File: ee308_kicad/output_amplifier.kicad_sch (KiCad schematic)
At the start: 39 parts, among them J1 Conn_Coaxial, Q1 2N3904, Q2 2N3904, Q3 2N3904, Q4 2N3906, Q5 2N3904, Q6 2N3904, Q7 2N3906

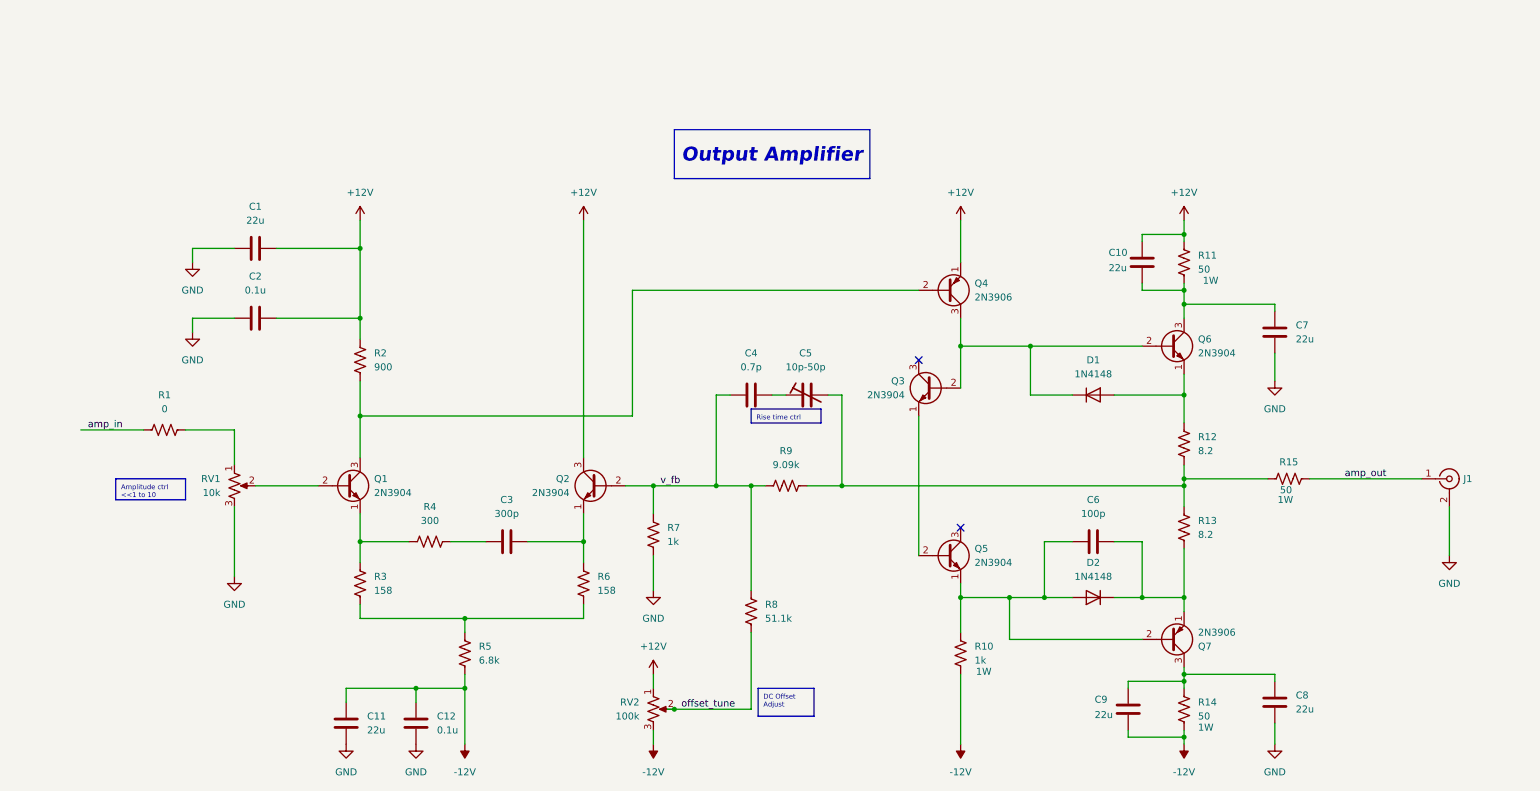
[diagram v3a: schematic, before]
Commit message: Update with current switch/integrator.
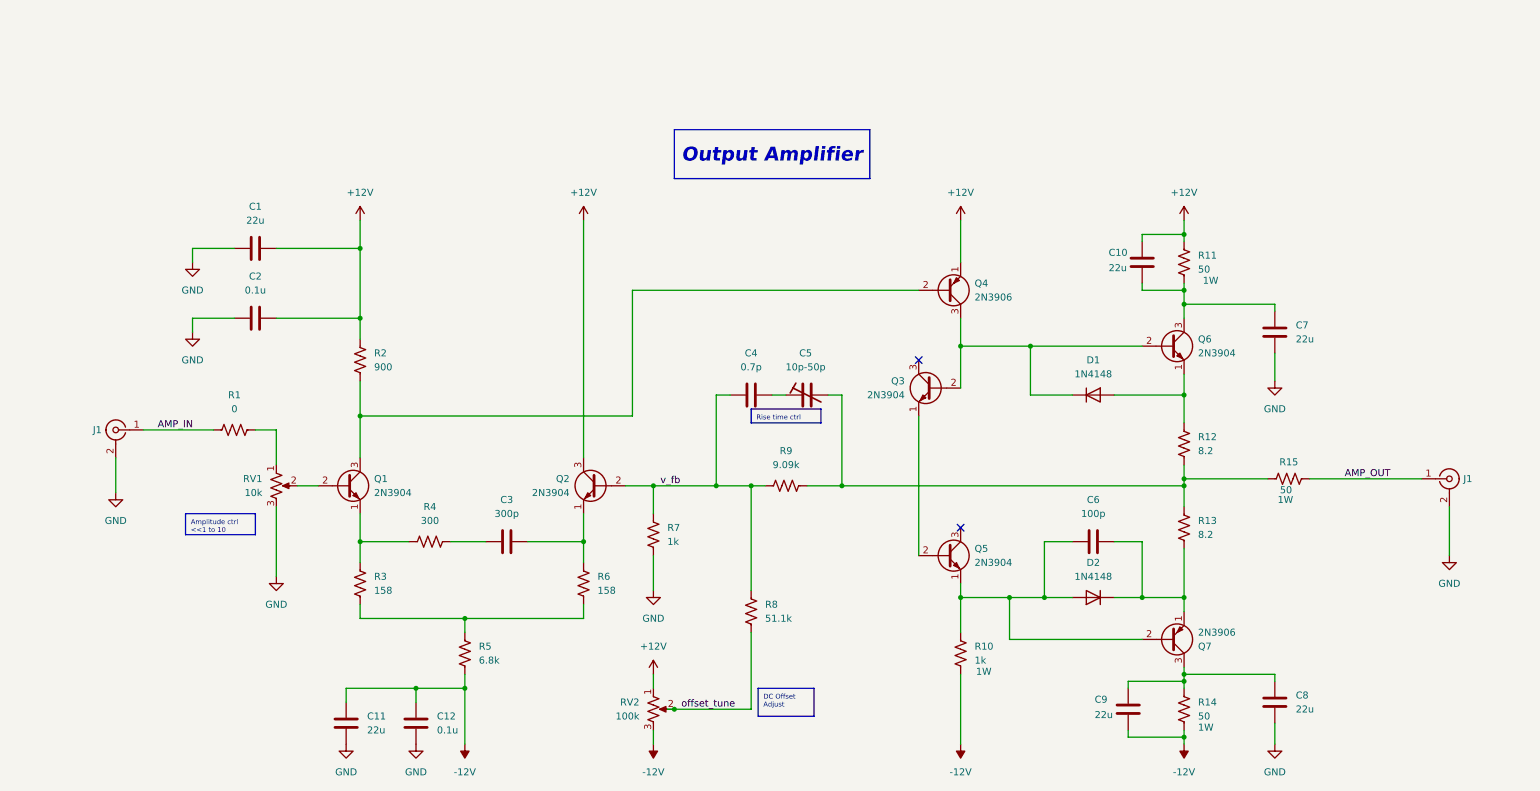
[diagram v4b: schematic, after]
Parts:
- added J1: Conn_Coaxial, Connector_Coaxial:SMA_Amphenol_901-143_Horizontal, symbol Connector:Conn_Coaxial
- J1: footprint Connector_Coaxial:BNC_TEConnectivity_1478035_Horizontal -> Connector_Coaxial:SMA_Amphenol_901-143_Horizontal
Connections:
- net GND: now also J1.2 (Ext)
- net amp_in renamed AMP_IN
- net AMP_IN: now also J1.1 (In)
- net amp_out renamed AMP_OUT
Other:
- moved on the sheet: R1, RV1
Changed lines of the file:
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@@
 	(text_box "Amplitude ctrl\n<<1 to 10"
 		(exclude_from_sim no)
-		(at 29.21 99.06 0)
+		(at 41.91 105.41 0)
 		(size 12.7 3.81)
 		(margins 0.9525 0.9525 0.9525 0.9525)
@@
 	(wire
 		(pts
-			(xy 50.8 90.17) (xy 50.8 96.52)
+			(xy 58.42 90.17) (xy 58.42 96.52)
 		)
 		(stroke
@@
 	(wire
 		(pts
-			(xy 22.86 90.17) (xy 34.29 90.17)
-		)
-		(stroke
-			(width 0)
-			(type default)
-		)
-	)
-	(wire
-		(pts
 			(xy 223.52 146.05) (xy 223.52 147.32)
 		)
@@
 	(wire
 		(pts
-			(xy 54.61 100.33) (xy 66.04 100.33)
+			(xy 62.23 100.33) (xy 66.04 100.33)
 		)
 		(stroke
@@
 	(wire
 		(pts
-			(xy 41.91 90.17) (xy 50.8 90.17)
+			(xy 34.29 90.17) (xy 46.99 90.17)
 		)
 		(stroke
@@
 	(wire
 		(pts
+			(xy 54.61 90.17) (xy 58.42 90.17)
+		)
+		(stroke
+			(width 0)
+			(type default)
+		)
+	)
+	(wire
+		(pts
 			(xy 114.3 105.41) (xy 114.3 110.49)
 		)
@@
 	(wire
 		(pts
-			(xy 50.8 104.14) (xy 50.8 116.84)
+			(xy 58.42 104.14) (xy 58.42 116.84)
 		)
 		(stroke
@@
 	(wire
 		(pts
+			(xy 29.21 95.25) (xy 29.21 101.6)
+		)
+		(stroke
+			(width 0)
+			(type default)
+		)
+	)
+	(wire
+		(pts
 			(xy 92.71 137.16) (xy 92.71 147.32)
 		)
@@
 		)
 	)
-	(label "amp_in"
-		(at 24.13 90.17 0)
+	(label "AMP_IN"
+		(at 36.83 90.17 0)
 		(effects
 			(font
@@
 		)
 	)
-	(label "amp_out"
+	(label "AMP_OUT"
 		(at 252.73 99.06 0)
 		(effects
@@
 	)
 	(symbol
+		(lib_id "Connector:Conn_Coaxial")
+		(at 29.21 90.17 0)
+		(mirror y)
+		(unit 1)
+		(exclude_from_sim no)
+		(in_bom yes)
+		(on_board yes)
+		(dnp no)
+		(property "Reference" "J1"
+			(at 26.67 90.17 0)
+			(effects
+				(font
+					(size 1.27 1.27)
+				)
+				(justify left)
+			)
+		)
+		(property "Value" "Conn_Coaxial"
+			(at 25.4 91.7331 0)
+			(effects
+				(font
+					(size 1.27 1.27)
+				)
+				(justify left)
+				(hide yes)
+			)
+		)
+		(property "Footprint" "Connector_Coaxial:SMA_Amphenol_901-143_Horizontal"
+			(at 29.21 90.17 0)
+			(effects
+				(font
+					(size 1.27 1.27)
+				)
+				(hide yes)
+			)
+		)
+		(property "Datasheet" "~"
+			(at 29.21 90.17 0)
+			(effects
+				(font
+					(size 1.27 1.27)
+				)
+				(hide yes)
+			)
+		)
+		(property "Description" "coaxial connector (BNC, SMA, SMB, SMC, Cinch/RCA, LEMO, ...)"
+			(at 29.21 90.17 0)
+			(effects
+				(font
+					(size 1.27 1.27)
+				)
+				(hide yes)
+			)
+		)
+		(pin "1"
+		)
+		(pin "2"
+		)
+		(instances
+			(project "ee308_kicad"
+				(path "/a3231158-6fd4-4190-9d01-56c0026ed088/88a04215-6888-4715-acfc-eedd1a2f0861"
+					(reference "J1")
+					(unit 1)
+				)
+			)
+		)
+	)
+	(symbol
 		(lib_id "power:GND")
 		(at 271.78 113.03 0)
@@
 	(symbol
 		(lib_id "power:GND")
-		(at 50.8 116.84 0)
+		(at 58.42 116.84 0)
 		(unit 1)
 		(exclude_from_sim no)
@@
 		(fields_autoplaced yes)
 		(property "Reference" "#PWR03"
-			(at 50.8 123.19 0)
+			(at 58.42 123.19 0)
 			(effects
 				(font
@@
 		)
 		(property "Value" "GND"
-			(at 50.8 121.92 0)
+			(at 58.42 121.92 0)
 			(effects
 				(font
@@
 		)
 		(property "Footprint" ""
-			(at 50.8 116.84 0)
+			(at 58.42 116.84 0)
 			(effects
 				(font
@@
 		)
 		(property "Datasheet" ""
-			(at 50.8 116.84 0)
+			(at 58.42 116.84 0)
 			(effects
 				(font
@@
 		)
 		(property "Description" "Power symbol creates a global label with name \"GND\" , ground"
-			(at 50.8 116.84 0)
+			(at 58.42 116.84 0)
 			(effects
 				(font
@@
 	(symbol
 		(lib_id "Device:R_Potentiometer_US")
-		(at 50.8 100.33 0)
+		(at 58.42 100.33 0)
 		(unit 1)
 		(exclude_from_sim no)
@@
 		(fields_autoplaced yes)
 		(property "Reference" "RV1"
-			(at 48.26 99.0599 0)
+			(at 55.88 99.0599 0)
 			(effects
 				(font
@@
 		)
 		(property "Value" "10k"
-			(at 48.26 101.5999 0)
+			(at 55.88 101.5999 0)
 			(effects
 				(font
@@
 		)
 		(property "Footprint" "Potentiometer_SMD:Potentiometer_ACP_CA6-VSMD_Vertical"
-			(at 50.8 100.33 0)
+			(at 58.42 100.33 0)
 			(effects
 				(font
@@
 		)
 		(property "Datasheet" "~"
-			(at 50.8 100.33 0)
+			(at 58.42 100.33 0)
 			(effects
 				(font
@@
 		)
 		(property "Description" "Potentiometer, US symbol"
-			(at 50.8 100.33 0)
+			(at 58.42 100.33 0)
 			(effects
 				(font
@@
 			)
 		)
-		(property "Footprint" "Connector_Coaxial:BNC_TEConnectivity_1478035_Horizontal"
+		(property "Footprint" "Connector_Coaxial:SMA_Amphenol_901-143_Horizontal"
 			(at 271.78 99.06 0)
 			(effects
@@
 	)
 	(symbol
+		(lib_id "power:GND")
+		(at 29.21 101.6 0)
+		(unit 1)
+		(exclude_from_sim no)
+		(in_bom yes)
+		(on_board yes)
+		(dnp no)
+		(fields_autoplaced yes)
+		(property "Reference" "#PWR035"
+			(at 29.21 107.95 0)
+			(effects
+				(font
+					(size 1.27 1.27)
+				)
+				(hide yes)
+			)
+		)
+		(property "Value" "GND"
+			(at 29.21 106.68 0)
+			(effects
+				(font
+					(size 1.27 1.27)
+				)
+			)
+		)
+		(property "Footprint" ""
+			(at 29.21 101.6 0)
+			(effects
+				(font
+					(size 1.27 1.27)
+				)
+				(hide yes)
+			)
+		)
+		(property "Datasheet" ""
+			(at 29.21 101.6 0)
+			(effects
+				(font
+					(size 1.27 1.27)
+				)
+				(hide yes)
+			)
+		)
+		(property "Description" "Power symbol creates a global label with name \"GND\" , ground"
+			(at 29.21 101.6 0)
+			(effects
+				(font
+					(size 1.27 1.27)
+				)
+				(hide yes)
+			)
+		)
+		(pin "1"
+		)
+		(instances
+			(project "ee308_kicad"
+				(path "/a3231158-6fd4-4190-9d01-56c0026ed088/88a04215-6888-4715-acfc-eedd1a2f0861"
+					(reference "#PWR035")
+					(unit 1)
+				)
+			)
+		)
+	)
+	(symbol
 		(lib_id "Device:R_US")
 		(at 223.52 140.97 0)
@@
 	(symbol
 		(lib_id "Device:R_US")
-		(at 38.1 90.17 270)
+		(at 50.8 90.17 270)
 		(unit 1)
 		(exclude_from_sim no)
@@
 		(fields_autoplaced yes)
 		(property "Reference" "R1"
-			(at 38.1 83.82 90)
+			(at 50.8 83.82 90)
 			(effects
 				(font
@@
 		)
 		(property "Value" "0"
-			(at 38.1 86.36 90)
+			(at 50.8 86.36 90)
 			(effects
 				(font
@@
 		)
 		(property "Footprint" "Resistor_SMD:R_0805_2012Metric_Pad1.20x1.40mm_HandSolder"
-			(at 37.846 91.186 90)
+			(at 50.546 91.186 90)
 			(effects
 				(font
@@
 		)
 		(property "Datasheet" "~"
-			(at 38.1 90.17 0)
+			(at 50.8 90.17 0)
 			(effects
 				(font
@@
 		)
 		(property "Description" "Resistor, US symbol"
-			(at 38.1 90.17 0)
+			(at 50.8 90.17 0)
 			(effects
 				(font
